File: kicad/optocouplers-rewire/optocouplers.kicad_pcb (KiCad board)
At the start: 2 copper layers, 123 parts, among them Q1 PN2222A, Q2 PN2222A, Q3 PN2222A, Q4 PN2222A, Q5 PN2222A, Q6 PN2222A, Q7 PN2222A, Q8 PN2222A

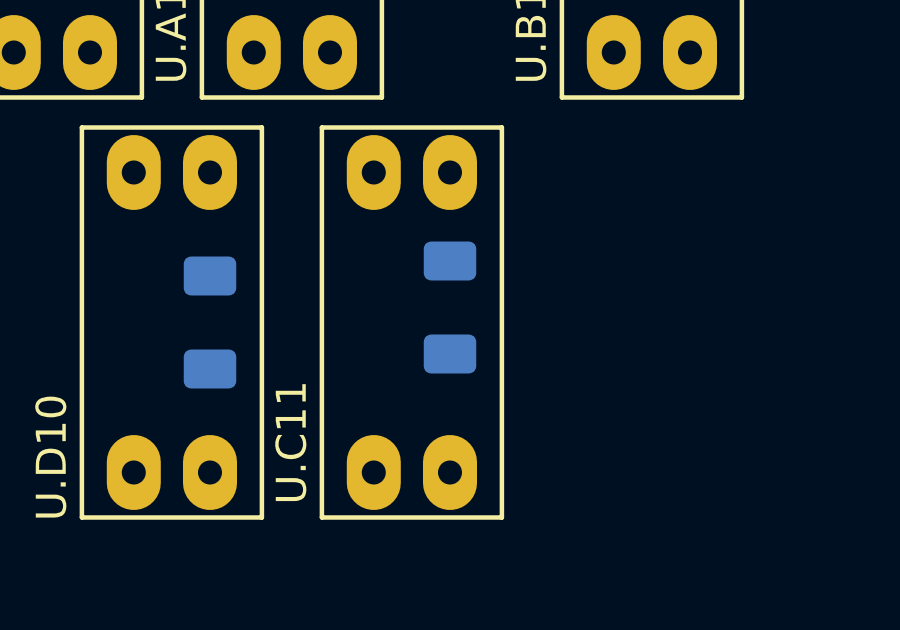
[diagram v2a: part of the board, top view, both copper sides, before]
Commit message: fix resistor location
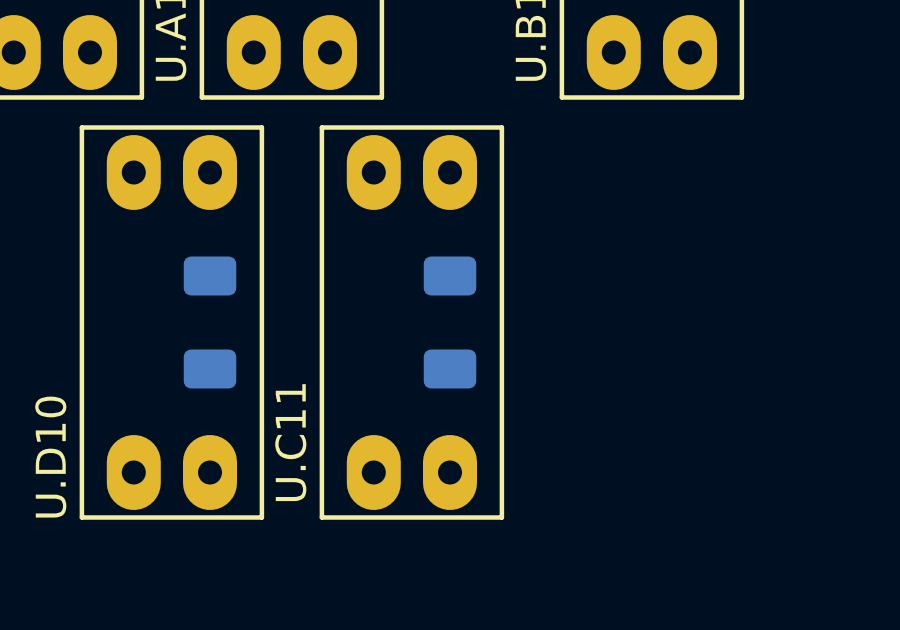
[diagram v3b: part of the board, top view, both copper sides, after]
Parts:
- moved R.C11 0.50 mm to (255.8, 48.5)
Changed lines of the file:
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@@
   )
   (footprint "Resistor_SMD:R_1206_3216Metric_Pad1.30x1.75mm_HandSolder" (layer "B.Cu")
-    (at 255.77 48 -90)
+    (at 255.77 48.5 -90)
     (descr "Resistor SMD 1206 (3216 Metric), square (rectangular) end terminal, IPC_7351 nominal with elongated pad for handsoldering. (Body size source: IPC-SM-782 page 72, https://www.pcb-3d.com/wordpress/wp-content/uploads/ipc-sm-782a_amendment_1_and_2.pdf), generated with kicad-footprint-generator")
     (tags "resistor handsolder")

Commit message: straight lines
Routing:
- net +5V: track 0.00 -> 460.0 mm
- net Net-(U.A6-Pad1): track 0.00 -> 3.45 mm
- net Net-(R.D9-Pad1): track 0.00 -> 3.45 mm
- net Net-(R.D8-Pad1): track 0.00 -> 3.45 mm
- net Net-(R.D7-Pad1): track 0.00 -> 3.45 mm
- net Net-(R.D6-Pad1): track 0.00 -> 3.45 mm
- net Net-(R.D5-Pad1): track 0.00 -> 3.45 mm
- net Net-(R.D4-Pad1): track 0.00 -> 3.45 mm
- net Net-(R.D3-Pad1): track 0.00 -> 3.45 mm
- net Net-(R.D2-Pad1): track 0.00 -> 3.45 mm
- net Net-(R.D10-Pad1): track 0.00 -> 3.45 mm
- net Net-(R.D1-Pad1): track 0.00 -> 3.45 mm
- net Net-(R.D0-Pad1): track 0.00 -> 3.45 mm
- net Net-(R.C9-Pad1): track 0.00 -> 3.45 mm
- net Net-(R.C8-Pad1): track 0.00 -> 3.45 mm
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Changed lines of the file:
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@@
     )
   )
+  (segment (start 23.77 36.05) (end 263.77 36.05) (width 0.6) (layer "B.Cu") (net 4))
+  (segment (start 35.77 50.05) (end 255.77 50.05) (width 0.6) (layer "B.Cu") (net 4))
+  (segment (start 31.77 29.5) (end 31.77 32.95) (width 0.6) (layer "B.Cu") (net 41))
+  (segment (start 51.77 29.5) (end 51.77 32.95) (width 0.6) (layer "B.Cu") (net 42))
+  (segment (start 71.77 29.5) (end 71.77 32.95) (width 0.6) (layer "B.Cu") (net 43))
+  (segment (start 91.77 29.5) (end 91.77 32.95) (width 0.6) (layer "B.Cu") (net 44))
+  (segment (start 111.77 29.5) (end 111.77 32.95) (width 0.6) (layer "B.Cu") (net 45))
+  (segment (start 131.77 29.5) (end 131.77 32.95) (width 0.6) (layer "B.Cu") (net 46))
+  (segment (start 151.77 29.5) (end 151.77 32.95) (width 0.6) (layer "B.Cu") (net 47))
+  (segment (start 171.77 29.5) (end 171.77 32.95) (width 0.6) (layer "B.Cu") (net 48))
+  (segment (start 191.77 29.5) (end 191.77 32.95) (width 0.6) (layer "B.Cu") (net 49))
+  (segment (start 211.77 29.5) (end 211.77 32.95) (width 0.6) (layer "B.Cu") (net 50))
+  (segment (start 231.77 29.5) (end 231.77 32.95) (width 0.6) (layer "B.Cu") (net 51))
+  (segment (start 251.77 29.5) (end 251.77 32.95) (width 0.6) (layer "B.Cu") (net 52))
+  (segment (start 23.77 29.5) (end 23.77 32.95) (width 0.6) (layer "B.Cu") (net 53))
+  (segment (start 43.77 29.5) (end 43.77 32.95) (width 0.6) (layer "B.Cu") (net 54))
+  (segment (start 63.77 29.5) (end 63.77 32.95) (width 0.6) (layer "B.Cu") (net 55))
+  (segment (start 83.77 29.5) (end 83.77 32.95) (width 0.6) (layer "B.Cu") (net 56))
+  (segment (start 103.77 29.5) (end 103.77 32.95) (width 0.6) (layer "B.Cu") (net 57))
+  (segment (start 123.77 29.5) (end 123.77 32.95) (width 0.6) (layer "B.Cu") (net 58))
+  (segment (start 143.77 29.5) (end 143.77 32.95) (width 0.6) (layer "B.Cu") (net 59))
+  (segment (start 163.77 29.5) (end 163.77 32.95) (width 0.6) (layer "B.Cu") (net 60))
+  (segment (start 183.77 29.5) (end 183.77 32.95) (width 0.6) (layer "B.Cu") (net 61))
+  (segment (start 203.77 29.5) (end 203.77 32.95) (width 0.6) (layer "B.Cu") (net 62))
+  (segment (start 223.77 29.5) (end 223.77 32.95) (width 0.6) (layer "B.Cu") (net 63))
+  (segment (start 243.77 29.5) (end 243.77 32.95) (width 0.6) (layer "B.Cu") (net 64))
+  (segment (start 263.77 29.5) (end 263.77 32.95) (width 0.6) (layer "B.Cu") (net 65))
+  (segment (start 35.77 43.5) (end 35.77 46.95) (width 0.6) (layer "B.Cu") (net 66))
+  (segment (start 55.77 43.5) (end 55.77 46.95) (width 0.6) (layer "B.Cu") (net 67))
+  (segment (start 75.77 43.5) (end 75.77 46.95) (width 0.6) (layer "B.Cu") (net 68))
+  (segment (start 95.77 43.5) (end 95.77 46.95) (width 0.6) (layer "B.Cu") (net 69))
+  (segment (start 115.77 43.5) (end 115.77 46.95) (width 0.6) (layer "B.Cu") (net 70))
+  (segment (start 135.77 43.5) (end 135.77 46.95) (width 0.6) (layer "B.Cu") (net 71))
+  (segment (start 155.77 43.5) (end 155.77 46.95) (width 0.6) (layer "B.Cu") (net 72))
+  (segment (start 175.77 43.5) (end 175.77 46.95) (width 0.6) (layer "B.Cu") (net 73))
+  (segment (start 195.77 43.5) (end 195.77 46.95) (width 0.6) (layer "B.Cu") (net 74))
+  (segment (start 215.77 43.5) (end 215.77 46.95) (width 0.6) (layer "B.Cu") (net 75))
+  (segment (start 235.77 43.5) (end 235.77 46.95) (width 0.6) (layer "B.Cu") (net 76))
+  (segment (start 255.77 43.5) (end 255.77 46.95) (width 0.6) (layer "B.Cu") (net 77))
+  (segment (start 47.77 43.5) (end 47.77 46.95) (width 0.6) (layer "B.Cu") (net 78))
+  (segment (start 67.77 43.5) (end 67.77 46.95) (width 0.6) (layer "B.Cu") (net 79))
+  (segment (start 87.77 43.5) (end 87.77 46.95) (width 0.6) (layer "B.Cu") (net 80))
+  (segment (start 107.77 43.5) (end 107.77 46.95) (width 0.6) (layer "B.Cu") (net 81))
+  (segment (start 127.77 43.5) (end 127.77 46.95) (width 0.6) (layer "B.Cu") (net 82))
+  (segment (start 147.77 43.5) (end 147.77 46.95) (width 0.6) (layer "B.Cu") (net 83))
+  (segment (start 167.77 43.5) (end 167.77 46.95) (width 0.6) (layer "B.Cu") (net 84))
+  (segment (start 187.77 43.5) (end 187.77 46.95) (width 0.6) (layer "B.Cu") (net 85))
+  (segment (start 207.77 43.5) (end 207.77 46.95) (width 0.6) (layer "B.Cu") (net 86))
+  (segment (start 227.77 43.5) (end 227.77 46.95) (width 0.6) (layer "B.Cu") (net 87))
+  (segment (start 247.77 43.5) (end 247.77 46.95) (width 0.6) (layer "B.Cu") (net 88))
   (zone (net 3) (net_name "GND") (layer "F.Cu") (hatch edge 0.508)
     (connect_pads (clearance 0.508))

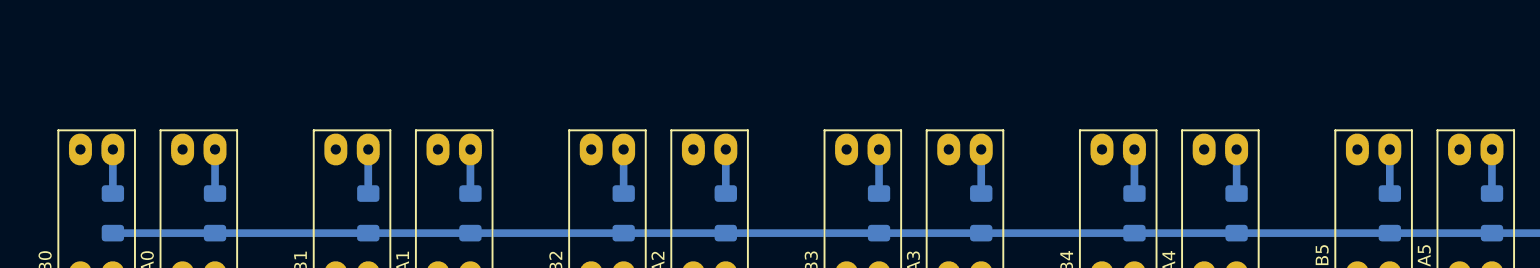
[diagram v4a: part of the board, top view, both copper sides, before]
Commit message: some nearly straight lines
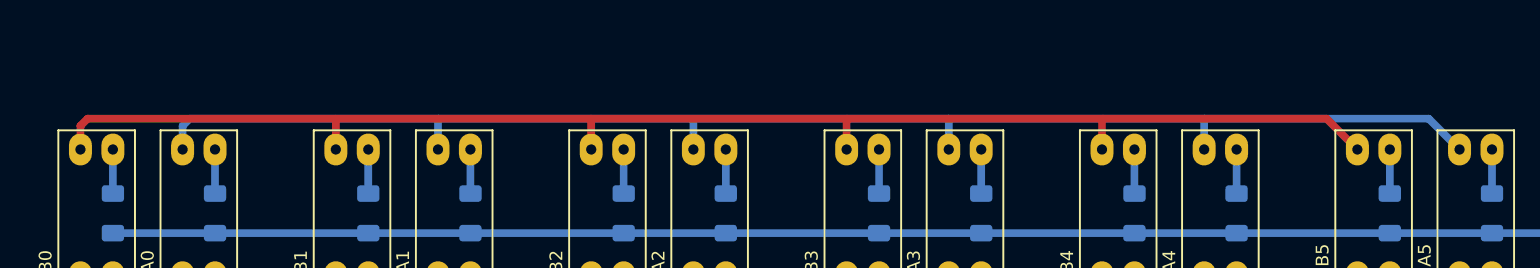
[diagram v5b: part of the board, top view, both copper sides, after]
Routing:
- net Net-(Q3-Pad3): track 0.00 -> 112.8 mm
- net Net-(Q1-Pad3): track 0.00 -> 112.8 mm
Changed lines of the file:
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@@
     )
   )
+  (segment (start 69.23 27.11) (end 69.206475 27.086475) (width 0.6) (layer "B.Cu") (net 2))
+  (segment (start 126.816475 27.086475) (end 129.23 29.5) (width 0.6) (layer "B.Cu") (net 2))
+  (segment (start 49.23 29.5) (end 49.23 27.11) (width 0.6) (layer "B.Cu") (net 2))
+  (segment (start 109.23 27.09) (end 109.233525 27.086475) (width 0.6) (layer "B.Cu") (net 2))
+  (segment (start 69.206475 27.086475) (end 89.233525 27.086475) (width 0.6) (layer "B.Cu") (net 2))
+  (segment (start 69.23 29.5) (end 69.23 27.11) (width 0.6) (layer "B.Cu") (net 2))
+  (segment (start 29.793525 27.086475) (end 49.253525 27.086475) (width 0.6) (layer "B.Cu") (net 2))
+  (segment (start 29.23 29.5) (end 29.23 27.65) (width 0.6) (layer "B.Cu") (net 2))
+  (segment (start 109.23 29.5) (end 109.23 27.09) (width 0.6) (layer "B.Cu") (net 2))
+  (segment (start 49.253525 27.086475) (end 69.206475 27.086475) (width 0.6) (layer "B.Cu") (net 2))
+  (segment (start 109.233525 27.086475) (end 126.816475 27.086475) (width 0.6) (layer "B.Cu") (net 2))
+  (segment (start 29.23 27.65) (end 29.793525 27.086475) (width 0.6) (layer "B.Cu") (net 2))
+  (segment (start 49.23 27.11) (end 49.253525 27.086475) (width 0.6) (layer "B.Cu") (net 2))
+  (segment (start 89.233525 27.086475) (end 109.233525 27.086475) (width 0.6) (layer "B.Cu") (net 2))
+  (segment (start 89.23 29.5) (end 89.23 27.09) (width 0.6) (layer "B.Cu") (net 2))
+  (segment (start 89.23 27.09) (end 89.233525 27.086475) (width 0.6) (layer "B.Cu") (net 2))
   (segment (start 23.77 36.05) (end 263.77 36.05) (width 0.6) (layer "B.Cu") (net 4))
   (segment (start 35.77 50.05) (end 255.77 50.05) (width 0.6) (layer "B.Cu") (net 4))
+  (segment (start 21.23 29.5) (end 21.23 27.65) (width 0.6) (layer "F.Cu") (net 22))
+  (segment (start 61.213525 27.086475) (end 81.233525 27.086475) (width 0.6) (layer "F.Cu") (net 22))
+  (segment (start 21.23 27.65) (end 21.793525 27.086475) (width 0.6) (layer "F.Cu") (net 22))
+  (segment (start 21.793525 27.086475) (end 41.206475 27.086475) (width 0.6) (layer "F.Cu") (net 22))
+  (segment (start 81.23 27.09) (end 81.233525 27.086475) (width 0.6) (layer "F.Cu") (net 22))
+  (segment (start 61.23 29.5) (end 61.23 27.10295) (width 0.6) (layer "F.Cu") (net 22))
+  (segment (start 101.23 27.16) (end 101.303525 27.086475) (width 0.6) (layer "F.Cu") (net 22))
+  (segment (start 41.23 29.5) (end 41.23 27.11) (width 0.6) (layer "F.Cu") (net 22))
+  (segment (start 61.23 27.10295) (end 61.213525 27.086475) (width 0.6) (layer "F.Cu") (net 22))
+  (segment (start 118.816475 27.086475) (end 121.23 29.5) (width 0.6) (layer "F.Cu") (net 22))
+  (segment (start 41.206475 27.086475) (end 61.213525 27.086475) (width 0.6) (layer "F.Cu") (net 22))
+  (segment (start 101.303525 27.086475) (end 118.816475 27.086475) (width 0.6) (layer "F.Cu") (net 22))
+  (segment (start 101.23 29.5) (end 101.23 27.16) (width 0.6) (layer "F.Cu") (net 22))
+  (segment (start 41.23 27.11) (end 41.206475 27.086475) (width 0.6) (layer "F.Cu") (net 22))
+  (segment (start 81.23 29.5) (end 81.23 27.09) (width 0.6) (layer "F.Cu") (net 22))
+  (segment (start 81.233525 27.086475) (end 101.303525 27.086475) (width 0.6) (layer "F.Cu") (net 22))
   (segment (start 31.77 29.5) (end 31.77 32.95) (width 0.6) (layer "B.Cu") (net 41))
   (segment (start 51.77 29.5) (end 51.77 32.95) (width 0.6) (layer "B.Cu") (net 42))

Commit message: Move optocouplers 1 mm higher (TODO: one resistor belongs to a different commit)
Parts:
- moved R.A0 1.30 mm to (31.8, 33.2)
- moved U.A0 1.00 mm to (30.5, 33.5)
- moved U.A1 1.00 mm to (50.5, 33.5)
- moved U.A10 1.00 mm to (230.5, 33.5)
- moved U.A11 1.00 mm to (250.5, 33.5)
- moved U.A2 1.00 mm to (70.5, 33.5)
- moved U.A3 1.00 mm to (90.5, 33.5)
- moved U.A4 1.00 mm to (110.5, 33.5)
- moved U.A5 1.00 mm to (130.5, 33.5)
- moved U.A6 1.00 mm to (150.5, 33.5)
- moved U.A7 1.00 mm to (170.5, 33.5)
- moved U.A8 1.00 mm to (190.5, 33.5)
- moved U.A9 1.00 mm to (210.5, 33.5)
- moved U.B0 1.00 mm to (22.5, 33.5)
- moved U.B1 1.00 mm to (42.5, 33.5)
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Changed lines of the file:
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@@
   (net 88 "Net-(R.D10-Pad1)")
   (footprint "ITR9608:ITR9608" (layer "F.Cu")
-    (at 30.5 34.5)
+    (at 30.5 33.5)
     (property "Sheetfile" "optocouplers.kicad_sch")
     (property "Sheetname" "")
@@
   )
   (footprint "ITR9608:ITR9608" (layer "F.Cu")
-    (at 50.5 34.5)
+    (at 50.5 33.5)
     (property "Sheetfile" "optocouplers.kicad_sch")
     (property "Sheetname" "")
@@
   )
   (footprint "ITR9608:ITR9608" (layer "F.Cu")
-    (at 70.5 34.5)
+    (at 70.5 33.5)
     (property "Sheetfile" "optocouplers.kicad_sch")
     (property "Sheetname" "")
@@
   )
   (footprint "ITR9608:ITR9608" (layer "F.Cu")
-    (at 90.5 34.5)
+    (at 90.5 33.5)
     (property "Sheetfile" "optocouplers.kicad_sch")
     (property "Sheetname" "")
@@
   )
   (footprint "ITR9608:ITR9608" (layer "F.Cu")
-    (at 110.5 34.5)
+    (at 110.5 33.5)
     (property "Sheetfile" "optocouplers.kicad_sch")
     (property "Sheetname" "")
@@
   )
   (footprint "ITR9608:ITR9608" (layer "F.Cu")
-    (at 130.5 34.5)
+    (at 130.5 33.5)
     (property "Sheetfile" "optocouplers.kicad_sch")
     (property "Sheetname" "")
@@
   )
   (footprint "ITR9608:ITR9608" (layer "F.Cu")
-    (at 150.5 34.5)
+    (at 150.5 33.5)
     (property "Sheetfile" "optocouplers.kicad_sch")
     (property "Sheetname" "")
@@
   )
   (footprint "ITR9608:ITR9608" (layer "F.Cu")
-    (at 170.5 34.5)
+    (at 170.5 33.5)
     (property "Sheetfile" "optocouplers.kicad_sch")
     (property "Sheetname" "")
@@
   )
   (footprint "ITR9608:ITR9608" (layer "F.Cu")
-    (at 190.5 34.5)
+    (at 190.5 33.5)
     (property "Sheetfile" "optocouplers.kicad_sch")
     (property "Sheetname" "")
@@
   )
   (footprint "ITR9608:ITR9608" (layer "F.Cu")
-    (at 210.5 34.5)
+    (at 210.5 33.5)
     (property "Sheetfile" "optocouplers.kicad_sch")
     (property "Sheetname" "")
@@
   )
   (footprint "ITR9608:ITR9608" (layer "F.Cu")
-    (at 230.5 34.5)
+    (at 230.5 33.5)
     (property "Sheetfile" "optocouplers.kicad_sch")
     (property "Sheetname" "")
@@
   )
   (footprint "ITR9608:ITR9608" (layer "F.Cu")
-    (at 250.5 34.5)
+    (at 250.5 33.5)
     (property "Sheetfile" "optocouplers.kicad_sch")
     (property "Sheetname" "")
@@
   )
   (footprint "ITR9608:ITR9608" locked (layer "F.Cu")
-    (at 22.5 34.5)
-    (property "Sheetfile" "optocouplers.kicad_sch")
-    (property "Sheetname" "")
-    (attr through_hole)
-    (fp_text reference "U.B0" (at -4 4.5 270) (layer "F.SilkS")
+    (at 22.5 33.5)
+    (property "Sheetfile" "optocouplers.kicad_sch")
+    (property "Sheetname" "")
+    (attr through_hole)
+    (fp_text reference "U.B0" (at -4 4.5 90) (layer "F.SilkS")
       (effects (font (size 1 1) (thickness 0.15)))
     )
@@
   )
   (footprint "ITR9608:ITR9608" (layer "F.Cu")
-    (at 42.5 34.5)
+    (at 42.5 33.5)
     (property "Sheetfile" "optocouplers.kicad_sch")
     (property "Sheetname" "")
@@
   )
   (footprint "ITR9608:ITR9608" (layer "F.Cu")
-    (at 62.5 34.5)
+    (at 62.5 33.5)
     (property "Sheetfile" "optocouplers.kicad_sch")
     (property "Sheetname" "")
@@
   )
   (footprint "ITR9608:ITR9608" (layer "F.Cu")
-    (at 82.5 34.5)
+    (at 82.5 33.5)
     (property "Sheetfile" "optocouplers.kicad_sch")
     (property "Sheetname" "")
@@
   )
   (footprint "ITR9608:ITR9608" (layer "F.Cu")
-    (at 102.5 34.5)
+    (at 102.5 33.5)
     (property "Sheetfile" "optocouplers.kicad_sch")
     (property "Sheetname" "")
@@
   )
   (footprint "ITR9608:ITR9608" (layer "F.Cu")
-    (at 122.5 34.5)
+    (at 122.5 33.5)
     (property "Sheetfile" "optocouplers.kicad_sch")
     (property "Sheetname" "")
@@
   )
   (footprint "ITR9608:ITR9608" locked (layer "F.Cu")
-    (at 142.5 34.5)
+    (at 142.5 33.5)
     (property "Sheetfile" "optocouplers.kicad_sch")
     (property "Sheetname" "")
@@
   )
   (footprint "ITR9608:ITR9608" (layer "F.Cu")
-    (at 162.5 34.5)
+    (at 162.5 33.5)
     (property "Sheetfile" "optocouplers.kicad_sch")
     (property "Sheetname" "")
@@
   )
   (footprint "ITR9608:ITR9608" (layer "F.Cu")
-    (at 182.5 34.5)
+    (at 182.5 33.5)
     (property "Sheetfile" "optocouplers.kicad_sch")
     (property "Sheetname" "")
@@
   )
   (footprint "ITR9608:ITR9608" (layer "F.Cu")
-    (at 202.5 34.5)
+    (at 202.5 33.5)
     (property "Sheetfile" "optocouplers.kicad_sch")
     (property "Sheetname" "")
@@
   )
   (footprint "ITR9608:ITR9608" (layer "F.Cu")
-    (at 222.5 34.5)
+    (at 222.5 33.5)
     (property "Sheetfile" "optocouplers.kicad_sch")
     (property "Sheetname" "")
@@
   )
   (footprint "ITR9608:ITR9608" (layer "F.Cu")
-    (at 242.5 34.5)
+    (at 242.5 33.5)
     (property "Sheetfile" "optocouplers.kicad_sch")
     (property "Sheetname" "")
@@
   )
   (footprint "ITR9608:ITR9608" (layer "F.Cu")
-    (at 262.5 34.5)
+    (at 262.5 33.5)
     (property "Sheetfile" "optocouplers.kicad_sch")
     (property "Sheetname" "")
@@
   )
   (footprint "Resistor_SMD:R_1206_3216Metric_Pad1.30x1.75mm_HandSolder" (layer "B.Cu")
-    (at 31.77 34.5 -90)
+    (at 31.77 33.2 -90)
     (descr "Resistor SMD 1206 (3216 Metric), square (rectangular) end terminal, IPC_7351 nominal with elongated pad for handsoldering. (Body size source: IPC-SM-782 page 72, https://www.pcb-3d.com/wordpress/wp-content/uploads/ipc-sm-782a_amendment_1_and_2.pdf), generated with kicad-footprint-generator")
     (tags "resistor handsolder")

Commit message: Move some resistors a bit
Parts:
- moved R.A1 1.30 mm to (51.8, 33.2)
- moved R.A10 1.30 mm to (231.8, 33.2)
- moved R.A11 1.30 mm to (251.8, 33.2)
- moved R.A2 1.30 mm to (71.8, 33.2)
- moved R.A3 1.30 mm to (91.8, 33.2)
- moved R.A4 1.30 mm to (111.8, 33.2)
- moved R.A5 1.30 mm to (131.8, 33.2)
- moved R.A6 1.30 mm to (151.8, 33.2)
- moved R.A7 1.30 mm to (171.8, 33.2)
- moved R.A8 1.30 mm to (191.8, 33.2)
- moved R.A9 1.30 mm to (211.8, 33.2)
- moved R.B0 1.30 mm to (23.8, 33.2)
- moved R.B1 1.30 mm to (43.8, 33.2)
- moved R.B10 1.30 mm to (223.8, 33.2)
- moved R.B11 1.30 mm to (243.8, 33.2)
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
